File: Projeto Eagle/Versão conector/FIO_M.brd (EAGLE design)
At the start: 15.8 x 21.5 mm, 4 parts, among them J1 CONECTOR

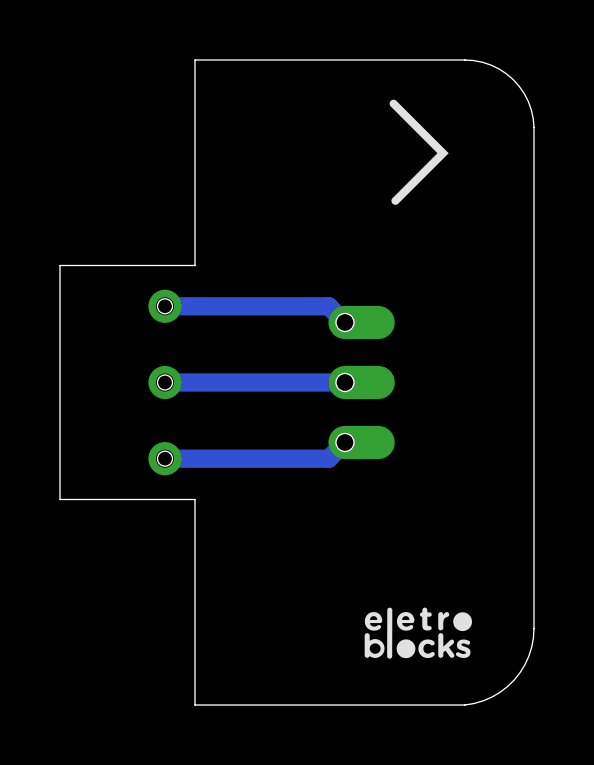
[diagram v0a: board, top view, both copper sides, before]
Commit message: correção de pads e adição de label de versionamento
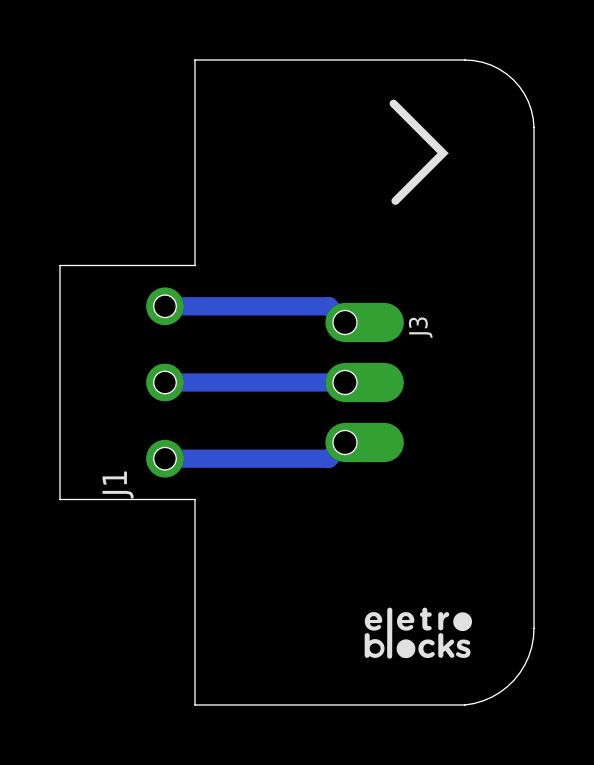
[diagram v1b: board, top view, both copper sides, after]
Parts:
- J1: value CONECTOR -> CONECTOR_MACHO
- renumbered U$2 to J3
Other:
- board text added: "V1.0.1"
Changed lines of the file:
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@@
 <grid distance="0.01" unitdist="mm" unit="mm" style="lines" multiple="1" display="yes" altdistance="0.01" altunitdist="mm" altunit="mm"/>
 <layers>
-<layer number="1" name="Top" color="4" fill="1" visible="no" active="yes"/>
+<layer number="1" name="Top" color="4" fill="1" visible="yes" active="yes"/>
 <layer number="2" name="Route2" color="16" fill="1" visible="no" active="no"/>
 <layer number="3" name="Route3" color="17" fill="1" visible="no" active="no"/>
@@
 <layer number="14" name="Route14" color="22" fill="1" visible="no" active="no"/>
 <layer number="15" name="Route15" color="23" fill="1" visible="no" active="no"/>
-<layer number="16" name="Bottom" color="1" fill="1" visible="no" active="yes"/>
+<layer number="16" name="Bottom" color="1" fill="1" visible="yes" active="yes"/>
 <layer number="17" name="Pads" color="2" fill="1" visible="yes" active="yes"/>
 <layer number="18" name="Vias" color="2" fill="1" visible="yes" active="yes"/>
 <layer number="19" name="Unrouted" color="6" fill="1" visible="yes" active="yes"/>
 <layer number="20" name="Dimension" color="24" fill="1" visible="yes" active="yes"/>
-<layer number="21" name="tPlace" color="7" fill="1" visible="no" active="yes"/>
+<layer number="21" name="tPlace" color="7" fill="1" visible="yes" active="yes"/>
 <layer number="22" name="bPlace" color="7" fill="1" visible="yes" active="yes"/>
 <layer number="23" name="tOrigins" color="15" fill="1" visible="yes" active="yes"/>
 <layer number="24" name="bOrigins" color="15" fill="1" visible="yes" active="yes"/>
-<layer number="25" name="tNames" color="7" fill="1" visible="no" active="yes"/>
+<layer number="25" name="tNames" color="7" fill="1" visible="yes" active="yes"/>
 <layer number="26" name="bNames" color="7" fill="1" visible="yes" active="yes"/>
 <layer number="27" name="tValues" color="7" fill="1" visible="no" active="yes"/>
@@
 <layer number="37" name="tTest" color="7" fill="1" visible="no" active="yes"/>
 <layer number="38" name="bTest" color="7" fill="1" visible="no" active="yes"/>
-<layer number="39" name="tKeepout" color="4" fill="11" visible="no" active="yes"/>
+<layer number="39" name="tKeepout" color="4" fill="11" visible="yes" active="yes"/>
 <layer number="40" name="bKeepout" color="1" fill="11" visible="yes" active="yes"/>
-<layer number="41" name="tRestrict" color="4" fill="10" visible="no" active="yes"/>
+<layer number="41" name="tRestrict" color="4" fill="10" visible="yes" active="yes"/>
 <layer number="42" name="bRestrict" color="1" fill="10" visible="yes" active="yes"/>
 <layer number="43" name="vRestrict" color="2" fill="10" visible="no" active="yes"/>
@@
 <layer number="48" name="Document" color="7" fill="1" visible="no" active="yes"/>
 <layer number="49" name="Reference" color="7" fill="1" visible="no" active="yes"/>
-<layer number="51" name="tDocu" color="7" fill="1" visible="no" active="yes"/>
+<layer number="51" name="tDocu" color="7" fill="1" visible="yes" active="yes"/>
 <layer number="52" name="bDocu" color="7" fill="1" visible="yes" active="yes"/>
 <layer number="88" name="SimResults" color="9" fill="1" visible="no" active="no"/>
@@
 <vertex x="2.50493125" y="2.1973375"/>
 </polygon>
+<text x="-1.18" y="21.32" size="0.6096" layer="22" font="fixed" rot="R270">V1.0.1</text>
 </plain>
 <attributes>
@@
 </groups>
 <elements>
-<element name="J1" library="Eletroblocks Lib" package="3CONECTOR" override_package3d_urn="urn:adsk.eagle:package:23100835/3" override_package_urn="urn:adsk.eagle:footprint:23100837/1" value="CONECTOR" x="-4.5" y="10.75" smashed="yes" grouprefs="BLOCO"/>
+<element name="J1" library="Eletroblocks Lib" package="3CONECTOR" override_package3d_urn="urn:adsk.eagle:package:23100835/3" override_package_urn="urn:adsk.eagle:footprint:23100837/1" override_locally_modified="yes" value="CONECTOR_MACHO" x="-4.5" y="10.75" smashed="yes" grouprefs="BLOCO">
+<attribute name="NAME" x="-5.77" y="6.94" size="0.8128" layer="21" font="fixed" rot="R90"/>
+</element>
 <element name="U$1" library="Eletroblocks Lib" package="PAD" value="PAD" x="1.5" y="12.75" smashed="yes"/>
-<element name="U$2" library="Eletroblocks Lib" package="PAD" override_package3d_urn="urn:adsk.eagle:package:23100844/2" override_package_urn="urn:adsk.eagle:footprint:23100847/1" value="PAD" x="1.5" y="10.75" smashed="yes"/>
+<element name="J3" library="Eletroblocks Lib" package="PAD" override_package3d_urn="urn:adsk.eagle:package:23100844/2" override_package_urn="urn:adsk.eagle:footprint:23100847/1" override_locally_modified="yes" value="PAD" x="1.5" y="10.75" smashed="yes">
+<attribute name="NAME" x="3.64" y="12.98" size="0.6096" layer="21" font="fixed" rot="R270"/>
+</element>
 <element name="VCC" library="Eletroblocks Lib" package="PAD" value="PAD" x="1.5" y="8.75" smashed="yes"/>
 </elements>
@@
 <signal name="SIGNAL_IN">
 <contactref element="J1" pad="2"/>
-<contactref element="U$2" pad="P$1"/>
+<contactref element="J3" pad="P$1"/>
 <wire x1="-4.5" y1="10.75" x2="1.5" y2="10.75" width="0.6096" layer="16"/>
 </signal>
